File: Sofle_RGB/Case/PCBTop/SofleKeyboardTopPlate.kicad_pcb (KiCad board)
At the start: 2 copper layers, 143.4 x 111.8 mm, 9 parts

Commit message: things
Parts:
- removed G*** (x4): LOGO, dane:gecko-logo
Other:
- net class Default removed
- rule pad_to_mask_clearance: 0.2 -> 0
- board text removed: "Original Sofle design by Josef Adamacik"
- board text removed: "Sofle RGB - Dane Evans"
- board text removed: "Sofle RGB v1.1, Dane Evans"
- board text removed: "https://josefadamcik.github.io/SofleKeyboard/"

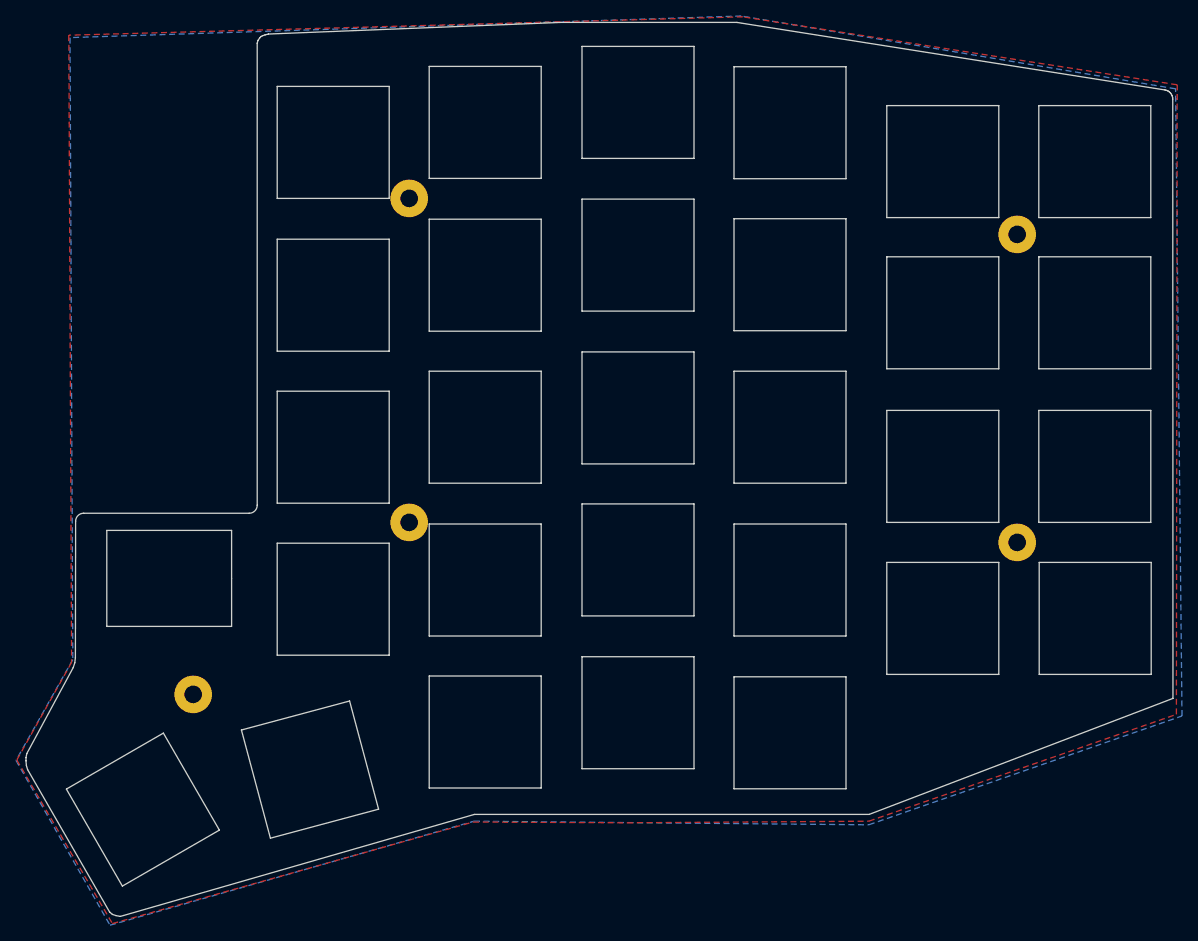
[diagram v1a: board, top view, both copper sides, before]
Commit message: fix: bottom holes
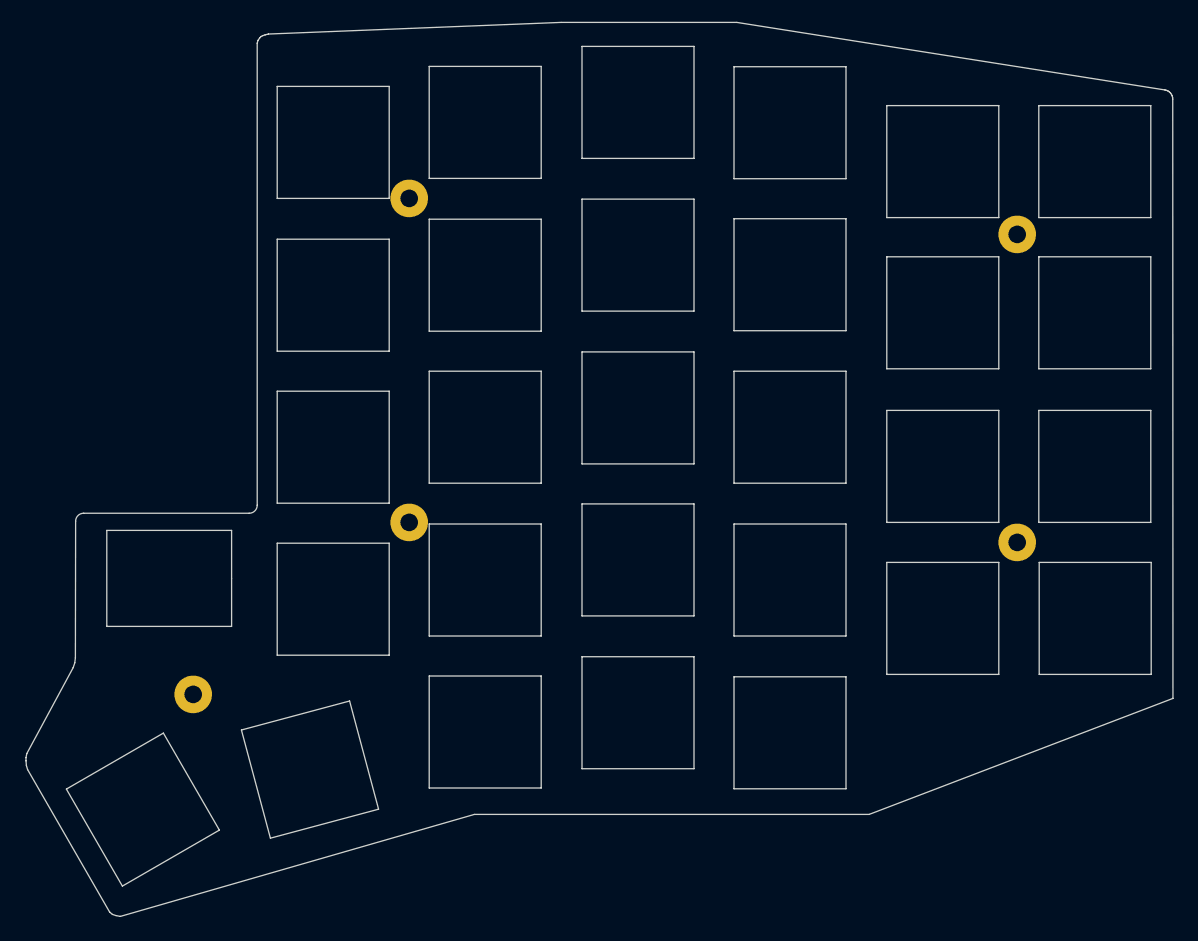
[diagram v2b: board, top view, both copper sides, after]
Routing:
- removed copper zone on B.Cu, net (none)
- removed copper zone on F.Cu, net (none)
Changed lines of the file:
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@@
   (gr_line (start 185.595 94.045) (end 171.595 94.045) (layer "Edge.Cuts") (width 0.15))
   (gr_line (start 128.495 115.545) (end 114.495 115.545) (layer "Edge.Cuts") (width 0.15))
-  (zone (net 0) (net_name "") (layer "F.Cu") (hatch edge 0.508)
-    (connect_pads (clearance 0.508))
-    (min_thickness 0.254) (filled_areas_thickness no)
-    (fill yes (thermal_gap 0.508) (thermal_bridge_width 0.508))
-    (polygon
-      (pts
-        (xy 81.945 128.645)
-        (xy 93.895 149.095)
-        (xy 138.995 136.395)
-        (xy 158.245 136.495)
-        (xy 188.445 136.295)
-        (xy 226.895 122.945)
-        (xy 226.995 44.245)
-        (xy 172.695 35.745)
-        (xy 88.445 38.045)
-        (xy 88.795 116.445)
-      )
-    )
-  )
-  (zone (net 0) (net_name "") (layer "B.Cu") (hatch edge 0.508)
-    (connect_pads (clearance 0.508))
-    (min_thickness 0.254) (filled_areas_thickness no)
-    (fill yes (thermal_gap 0.508) (thermal_bridge_width 0.508))
-    (polygon
-      (pts
-        (xy 81.845 128.695)
-        (xy 93.595 149.295)
-        (xy 139.095 136.295)
-        (xy 188.445 136.745)
-        (xy 227.595 123.145)
-        (xy 226.795 44.745)
-        (xy 172.495 35.645)
-        (xy 88.595 38.345)
-        (xy 88.945 116.095)
-      )
-    )
-  )
 )
